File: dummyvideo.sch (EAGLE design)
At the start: 12 parts, among them IC1 NE555

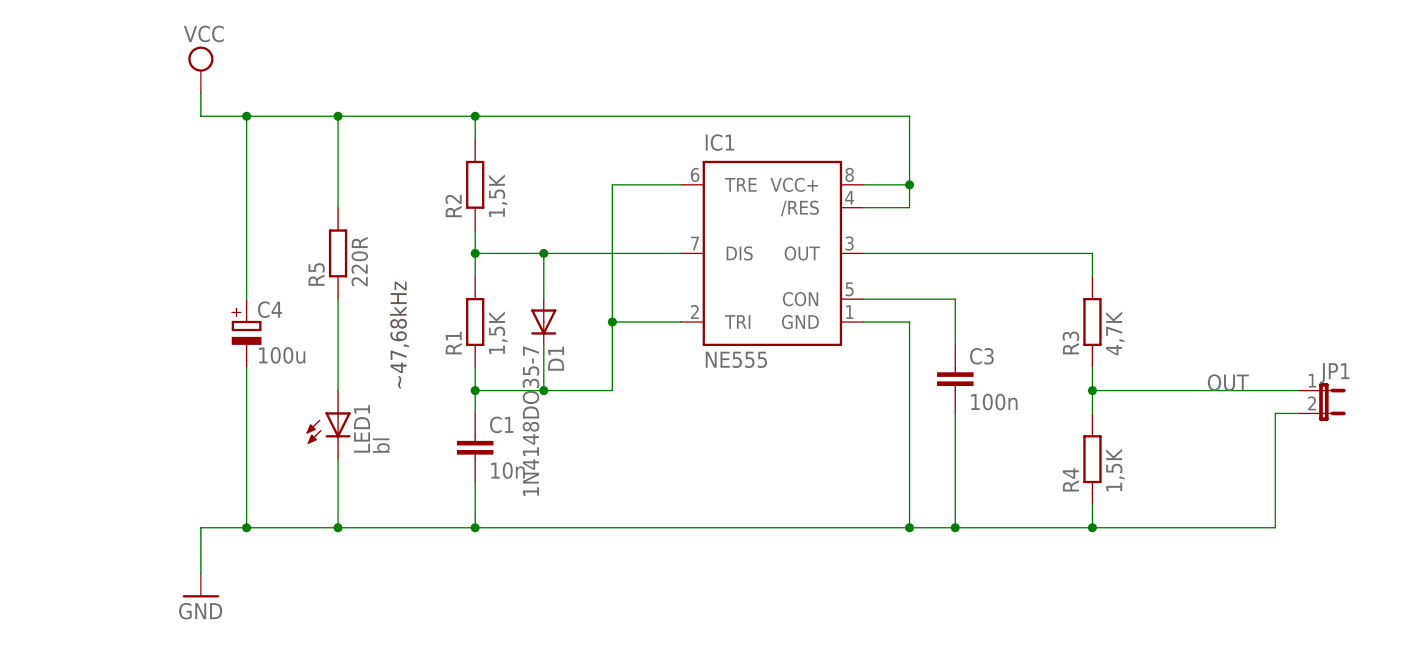
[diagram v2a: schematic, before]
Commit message: Added power and mount holes.
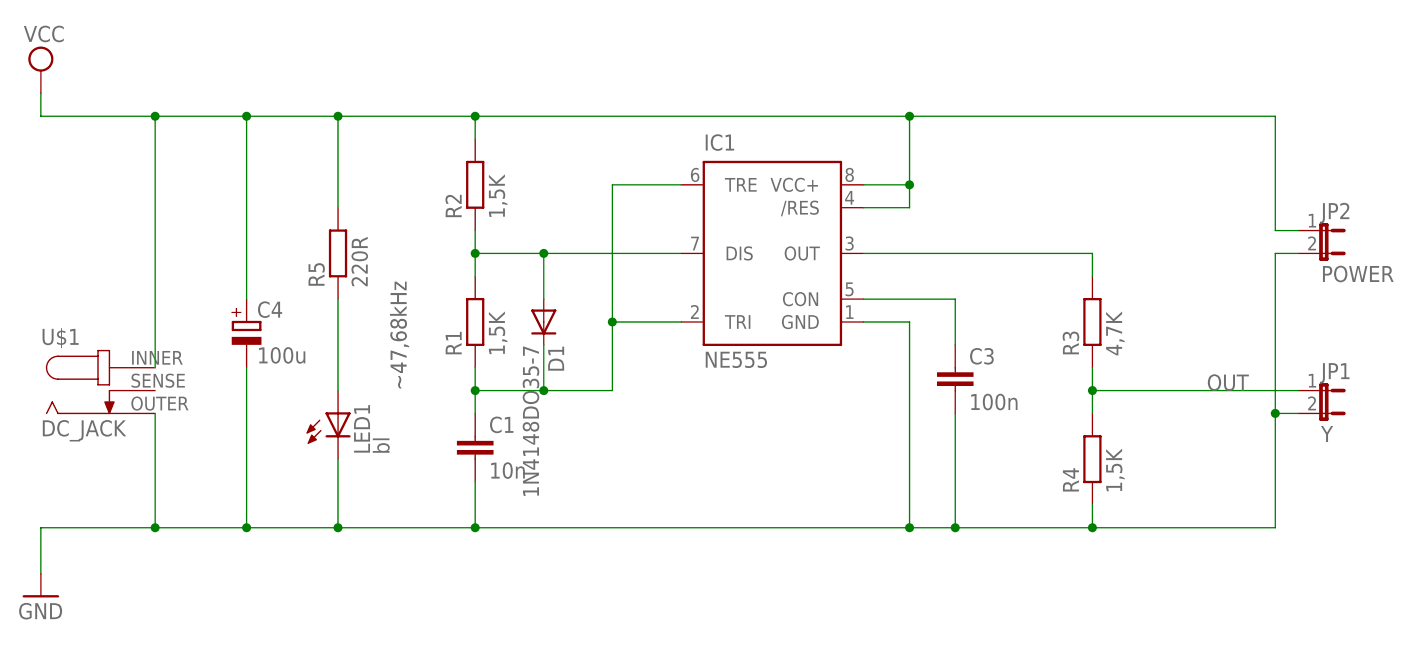
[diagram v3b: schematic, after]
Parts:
- added JP2: POWER, jumper:JP1E
- added U$1: DC_JACK, n39:DC_JACK
- JP1: value (none) -> Y
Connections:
- net GND: now also JP2.2, U$1.1
- net VCC: now also JP2.1, U$1.3
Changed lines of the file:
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@@
 <grid distance="0.1" unitdist="inch" unit="inch" style="lines" multiple="1" display="no" altdistance="0.01" altunitdist="inch" altunit="inch"/>
 <layers>
-<layer number="1" name="Top" color="4" fill="1" visible="yes" active="no"/>
-<layer number="16" name="Bottom" color="1" fill="1" visible="yes" active="no"/>
-<layer number="17" name="Pads" color="2" fill="1" visible="yes" active="no"/>
-<layer number="18" name="Vias" color="2" fill="1" visible="yes" active="no"/>
-<layer number="19" name="Unrouted" color="6" fill="1" visible="yes" active="no"/>
-<layer number="20" name="Dimension" color="15" fill="1" visible="yes" active="no"/>
-<layer number="21" name="tPlace" color="7" fill="1" visible="yes" active="no"/>
-<layer number="22" name="bPlace" color="7" fill="1" visible="yes" active="no"/>
-<layer number="23" name="tOrigins" color="15" fill="1" visible="yes" active="no"/>
-<layer number="24" name="bOrigins" color="15" fill="1" visible="yes" active="no"/>
-<layer number="25" name="tNames" color="7" fill="1" visible="yes" active="no"/>
-<layer number="26" name="bNames" color="7" fill="1" visible="yes" active="no"/>
-<layer number="27" name="tValues" color="7" fill="1" visible="yes" active="no"/>
-<layer number="28" name="bValues" color="7" fill="1" visible="yes" active="no"/>
+<layer number="1" name="Top" color="4" fill="1" visible="no" active="no"/>
+<layer number="16" name="Bottom" color="1" fill="1" visible="no" active="no"/>
+<layer number="17" name="Pads" color="2" fill="1" visible="no" active="no"/>
+<layer number="18" name="Vias" color="2" fill="1" visible="no" active="no"/>
+<layer number="19" name="Unrouted" color="6" fill="1" visible="no" active="no"/>
+<layer number="20" name="Dimension" color="15" fill="1" visible="no" active="no"/>
+<layer number="21" name="tPlace" color="7" fill="1" visible="no" active="no"/>
+<layer number="22" name="bPlace" color="7" fill="1" visible="no" active="no"/>
+<layer number="23" name="tOrigins" color="15" fill="1" visible="no" active="no"/>
+<layer number="24" name="bOrigins" color="15" fill="1" visible="no" active="no"/>
+<layer number="25" name="tNames" color="7" fill="1" visible="no" active="no"/>
+<layer number="26" name="bNames" color="7" fill="1" visible="no" active="no"/>
+<layer number="27" name="tValues" color="7" fill="1" visible="no" active="no"/>
+<layer number="28" name="bValues" color="7" fill="1" visible="no" active="no"/>
 <layer number="29" name="tStop" color="7" fill="3" visible="no" active="no"/>
 <layer number="30" name="bStop" color="7" fill="6" visible="no" active="no"/>
@@
 <layer number="35" name="tGlue" color="7" fill="4" visible="no" active="no"/>
 <layer number="36" name="bGlue" color="7" fill="5" visible="no" active="no"/>
-<layer number="37" name="tTest" color="7" fill="1" visible="yes" active="no"/>
-<layer number="38" name="bTest" color="7" fill="1" visible="yes" active="no"/>
+<layer number="37" name="tTest" color="7" fill="1" visible="no" active="no"/>
+<layer number="38" name="bTest" color="7" fill="1" visible="no" active="no"/>
 <layer number="39" name="tKeepout" color="4" fill="11" visible="no" active="no"/>
 <layer number="40" name="bKeepout" color="1" fill="11" visible="no" active="no"/>
@@
 <layer number="44" name="Drills" color="7" fill="1" visible="no" active="no"/>
 <layer number="45" name="Holes" color="7" fill="1" visible="no" active="no"/>
-<layer number="46" name="Milling" color="3" fill="1" visible="yes" active="no"/>
-<layer number="47" name="Measures" color="7" fill="1" visible="yes" active="no"/>
-<layer number="48" name="Document" color="7" fill="1" visible="yes" active="no"/>
-<layer number="49" name="Reference" color="7" fill="1" visible="yes" active="no"/>
-<layer number="51" name="tDocu" color="6" fill="1" visible="yes" active="no"/>
-<layer number="52" name="bDocu" color="7" fill="1" visible="yes" active="no"/>
+<layer number="46" name="Milling" color="3" fill="1" visible="no" active="no"/>
+<layer number="47" name="Measures" color="7" fill="1" visible="no" active="no"/>
+<layer number="48" name="Document" color="7" fill="1" visible="no" active="no"/>
+<layer number="49" name="Reference" color="7" fill="1" visible="no" active="no"/>
+<layer number="51" name="tDocu" color="6" fill="1" visible="no" active="no"/>
+<layer number="52" name="bDocu" color="7" fill="1" visible="no" active="no"/>
 <layer number="91" name="Nets" color="2" fill="1" visible="yes" active="yes"/>
 <layer number="92" name="Busses" color="1" fill="1" visible="yes" active="yes"/>
@@
 <part name="LED1" library="led" deviceset="LED" device="3MM" value="bl"/>
 <part name="R5" library="resistor" deviceset="R-EU_" device="0207/10" value="220R"/>
-<part name="JP1" library="jumper" deviceset="JP1E" device=""/>
+<part name="JP1" library="jumper" deviceset="JP1E" device="" value="Y"/>
+<part name="U$1" library="n39" deviceset="DC_JACK" device=""/>
+<part name="JP2" library="jumper" deviceset="JP1E" device="" value="POWER"/>
 </parts>
 <sheets>
@@
 <instances>
 <instance part="IC1" gate="G$1" x="55.88" y="58.42"/>
-<instance part="GND1" gate="1" x="-7.62" y="20.32"/>
-<instance part="SUPPLY1" gate="G$1" x="-7.62" y="78.74"/>
+<instance part="GND1" gate="1" x="-25.4" y="20.32"/>
+<instance part="SUPPLY1" gate="G$1" x="-25.4" y="78.74"/>
 <instance part="C4" gate="G$1" x="-2.54" y="50.8"/>
 <instance part="C3" gate="G$1" x="76.2" y="45.72"/>
@@
 <instance part="R5" gate="G$1" x="7.62" y="58.42" rot="R90"/>
 <instance part="JP1" gate="A" x="116.84" y="43.18" rot="R270"/>
+<instance part="U$1" gate="DC-PLUG" x="-17.78" y="43.18"/>
+<instance part="JP2" gate="A" x="116.84" y="60.96" rot="R270"/>
 </instances>
 <busses>
@@
 <pinref part="SUPPLY1" gate="G$1" pin="VCC"/>
 <wire x1="7.62" y1="73.66" x2="-2.54" y2="73.66" width="0.1524" layer="91"/>
-<wire x1="-2.54" y1="73.66" x2="-7.62" y2="73.66" width="0.1524" layer="91"/>
-<wire x1="-7.62" y1="73.66" x2="-7.62" y2="76.2" width="0.1524" layer="91"/>
+<wire x1="-2.54" y1="73.66" x2="-12.7" y2="73.66" width="0.1524" layer="91"/>
+<wire x1="-12.7" y1="73.66" x2="-25.4" y2="73.66" width="0.1524" layer="91"/>
+<wire x1="-25.4" y1="73.66" x2="-25.4" y2="76.2" width="0.1524" layer="91"/>
 <pinref part="C4" gate="G$1" pin="+"/>
 <wire x1="-2.54" y1="53.34" x2="-2.54" y2="73.66" width="0.1524" layer="91"/>
@@
 <wire x1="7.62" y1="63.5" x2="7.62" y2="73.66" width="0.1524" layer="91"/>
 <junction x="7.62" y="73.66"/>
+<pinref part="U$1" gate="DC-PLUG" pin="3"/>
+<wire x1="-12.7" y1="45.72" x2="-12.7" y2="73.66" width="0.1524" layer="91"/>
+<junction x="-12.7" y="73.66"/>
+<wire x1="71.12" y1="73.66" x2="111.76" y2="73.66" width="0.1524" layer="91"/>
+<wire x1="111.76" y1="73.66" x2="111.76" y2="60.96" width="0.1524" layer="91"/>
+<junction x="71.12" y="73.66"/>
+<pinref part="JP2" gate="A" pin="1"/>
+<wire x1="111.76" y1="60.96" x2="114.3" y2="60.96" width="0.1524" layer="91"/>
 </segment>
 </net>
@@
 <pinref part="GND1" gate="1" pin="GND"/>
 <wire x1="7.62" y1="27.94" x2="-2.54" y2="27.94" width="0.1524" layer="91"/>
-<wire x1="-2.54" y1="27.94" x2="-7.62" y2="27.94" width="0.1524" layer="91"/>
-<wire x1="-7.62" y1="27.94" x2="-7.62" y2="22.86" width="0.1524" layer="91"/>
+<wire x1="-2.54" y1="27.94" x2="-12.7" y2="27.94" width="0.1524" layer="91"/>
+<wire x1="-12.7" y1="27.94" x2="-25.4" y2="27.94" width="0.1524" layer="91"/>
+<wire x1="-25.4" y1="27.94" x2="-25.4" y2="22.86" width="0.1524" layer="91"/>
 <pinref part="C4" gate="G$1" pin="-"/>
 <wire x1="-2.54" y1="45.72" x2="-2.54" y2="27.94" width="0.1524" layer="91"/>
@@
 <wire x1="111.76" y1="27.94" x2="91.44" y2="27.94" width="0.1524" layer="91"/>
 <junction x="91.44" y="27.94"/>
+<pinref part="U$1" gate="DC-PLUG" pin="1"/>
+<wire x1="-12.7" y1="40.64" x2="-12.7" y2="27.94" width="0.1524" layer="91"/>
+<junction x="-12.7" y="27.94"/>
+<wire x1="111.76" y1="40.64" x2="111.76" y2="58.42" width="0.1524" layer="91"/>
+<junction x="111.76" y="40.64"/>
+<pinref part="JP2" gate="A" pin="2"/>
+<wire x1="111.76" y1="58.42" x2="114.3" y2="58.42" width="0.1524" layer="91"/>
 </segment>
 </net>

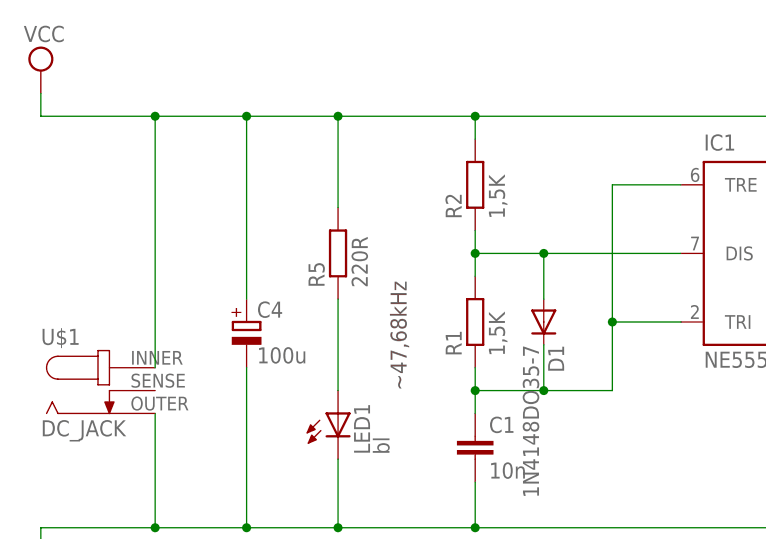
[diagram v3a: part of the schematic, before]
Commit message: Wiederstand vor der LED angepasst
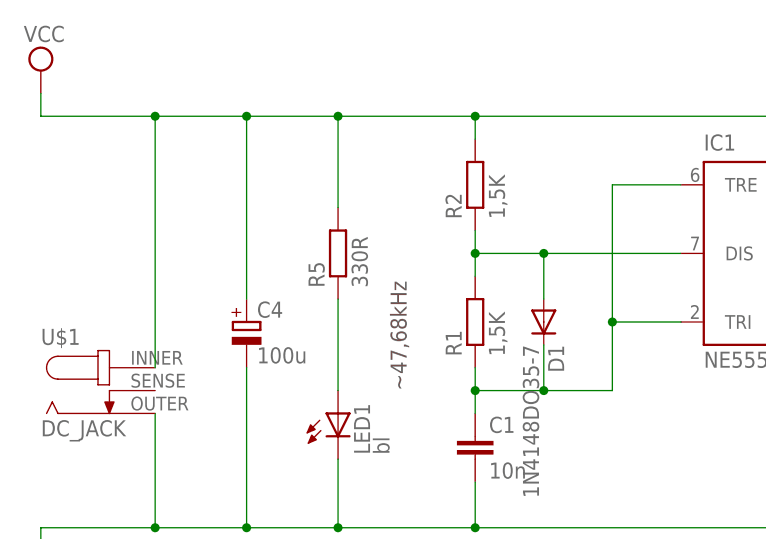
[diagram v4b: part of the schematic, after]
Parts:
- R5: value 220R -> 330R
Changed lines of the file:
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@@
 <part name="R4" library="resistor" deviceset="R-EU_" device="0207/10" value="1,5K"/>
 <part name="LED1" library="led" deviceset="LED" device="3MM" value="bl"/>
-<part name="R5" library="resistor" deviceset="R-EU_" device="0207/10" value="220R"/>
+<part name="R5" library="resistor" deviceset="R-EU_" device="0207/10" value="330R"/>
 <part name="JP1" library="jumper" deviceset="JP1E" device="" value="Y"/>
 <part name="U$1" library="n39" deviceset="DC_JACK" device=""/>

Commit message: First revision of SMD board
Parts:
- removed JP1: Y, jumper:JP1E
- removed JP2: POWER, jumper:JP1E
- removed U$1: DC_JACK, n39:DC_JACK
- added JP_PAD1, JP_PAD2, PAD_Y, PWR_PAD_GND, PWR_PAD_VCC: (no value), wirepad:SMD2
- C1, C3: device resistor:C-EU025-025X050 -> resistor:C-EUC0805
- C4: value 100u -> 47u; device resistor:CPOL-EUE15-6AXIAL -> resistor:CPOL-EU153CLV-0505
- IC1: value NE555 -> NE555SO; device st-microelectronics:NE555 -> n39:NE555SO
- LED1: value bl -> gn LC; device led:LED3MM -> led:LEDCHIPLED-0603-TTW
- R1, R3, R4: device resistor:R-EU_0207/10 -> resistor:R-EU_R0805
- R2: device resistor:R-EU_0207/10 -> resistor:R-EU_M0805
- R5: value 330R -> 1,5K; device resistor:R-EU_0207/10 -> resistor:R-EU_R0805
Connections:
- new net N$6: JP_PAD2.P, PWR_PAD_VCC.P
- net GND: now also PWR_PAD_GND.P; no longer JP1.2, JP2.2, U$1.1
- net OUT: now also PAD_Y.P; no longer JP1.1
- net VCC: now also JP_PAD1.P; no longer JP2.1, U$1.3
